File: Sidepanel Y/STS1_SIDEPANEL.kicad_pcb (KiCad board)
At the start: 4 copper layers, 82.8 x 100 mm, 47 parts, among them IC1 TMP112AQDRLRQ1, J1 Conn_01x08, U1 GUVA-C32SM, U11 INA180A4, U12 INA180A4

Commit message: Changed the values of the VCTRL resistors.
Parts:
- R61, R62: value 1M -> 3k
- R71, R72: value 330k -> 1k

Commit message: Updated according to the review from Dhruva.
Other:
- outline, holes or cut-outs redrawn
- board text added: "Y+ v3.0"
- board text removed: "Y+ v2.5"

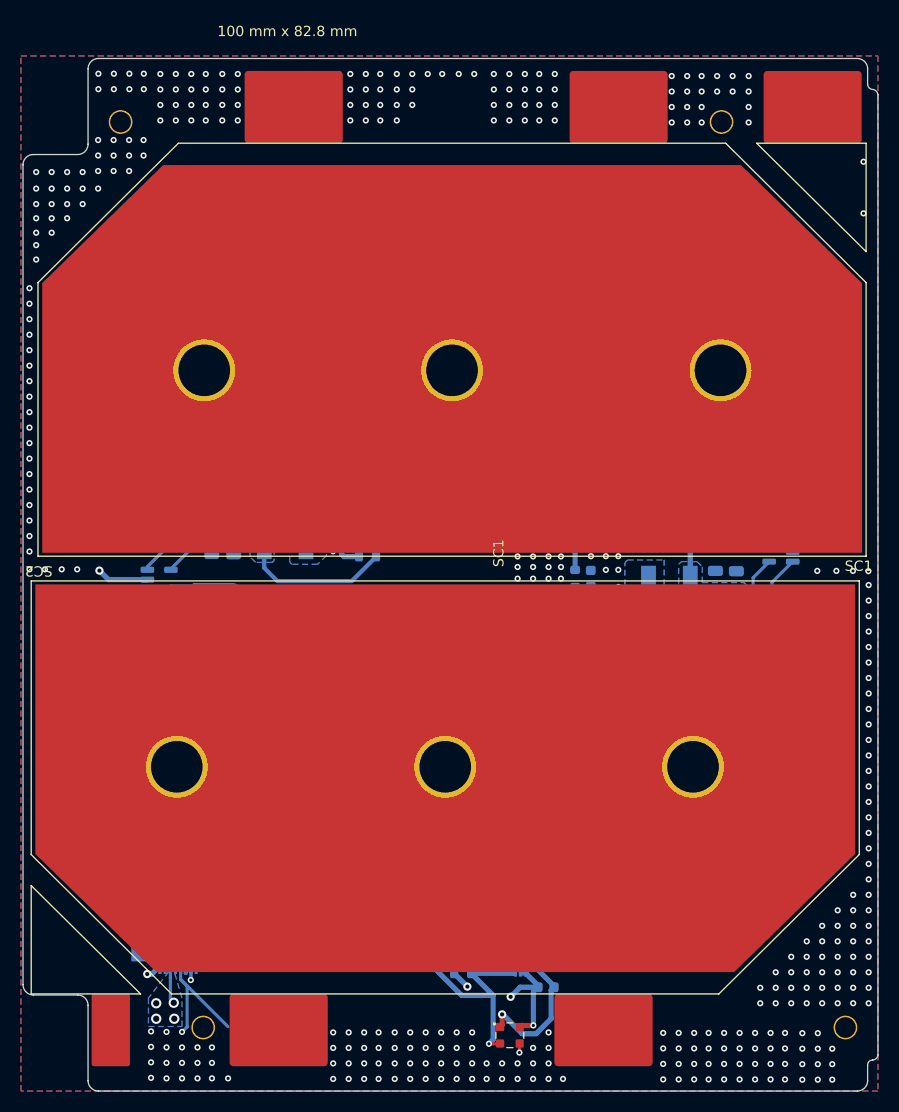
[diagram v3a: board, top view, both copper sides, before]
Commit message: changed all vias from blind to trough and removed the unused pins of the uci connector
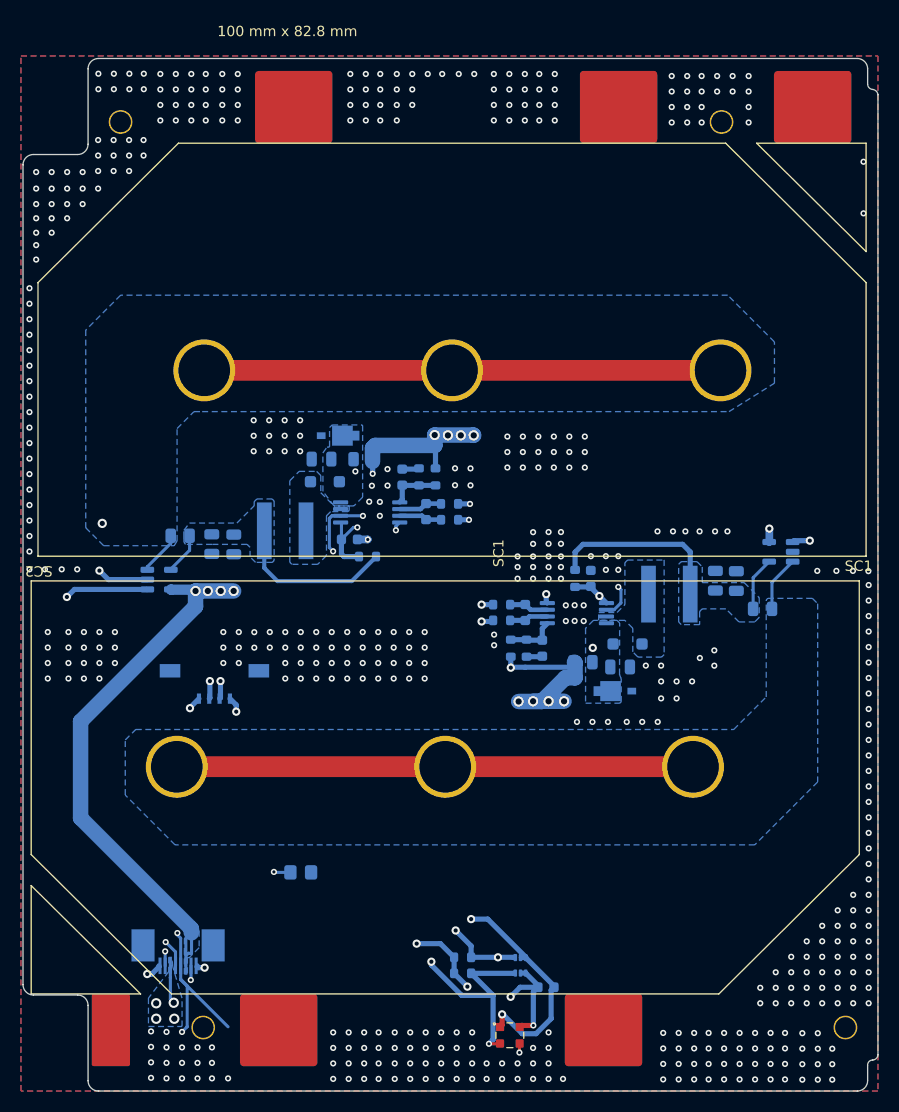
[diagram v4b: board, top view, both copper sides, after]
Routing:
- net /SC2_V+: track 28.3 -> 78.3 mm
- net /SC1_V+: track 66.4 -> 109.0 mm

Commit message: chaned the connectors for the cameras from buttom to top contact
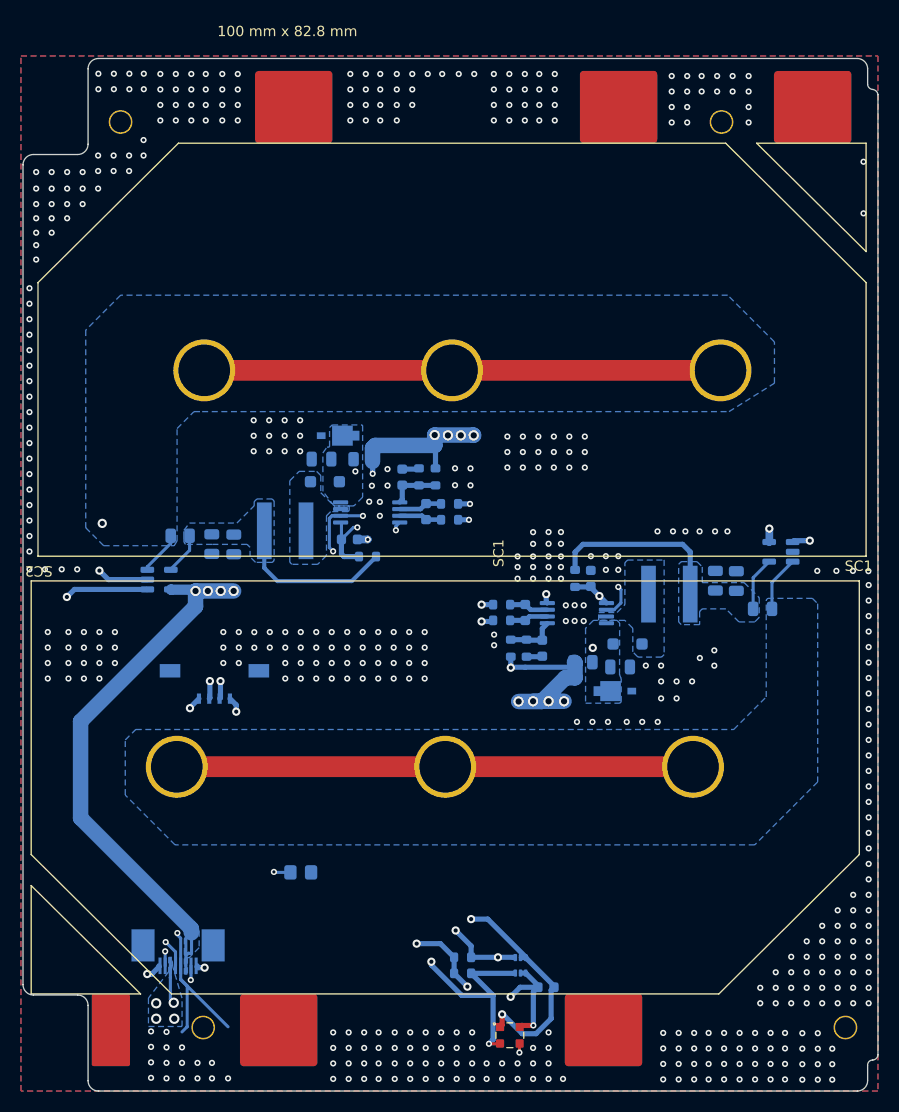
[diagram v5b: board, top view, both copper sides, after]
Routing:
- net GND: vias 505 -> 497
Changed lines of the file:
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@@
-	)
-	(via
-		(at 149.325 45.7)
-		(size 0.6)
-		(drill 0.3)
-		(layers "F.Cu" "B.Cu")
-		(free yes)
-		(net 1)
 	)
 	(via
@@
 	)
 	(via
-		(at 99 133.775)
-		(size 0.6)
-		(drill 0.3)
-		(layers "F.Cu" "B.Cu")
-		(free yes)
-		(net 1)
-	)
-	(via
 		(at 147.925 44.2)
 		(size 0.6)
@@
 	)
 	(via
-		(at 93.875 47.4)
-		(size 0.6)
-		(drill 0.3)
-		(layers "F.Cu" "B.Cu")
-		(free yes)
-		(net 1)
-	)
-	(via
 		(at 152.325 42.7)
 		(size 0.6)
@@
 	)
 	(via
-		(at 149.325 44.2)
-		(size 0.6)
-		(drill 0.3)
-		(layers "F.Cu" "B.Cu")
-		(free yes)
-		(net 1)
-	)
-	(via
 		(at 101.9 138.275)
 		(size 0.6)
@@
 	)
 	(via
-		(at 90.875 47.4)
-		(size 0.6)
-		(drill 0.3)
-		(layers "F.Cu" "B.Cu")
-		(free yes)
-		(net 1)
-	)
-	(via
 		(at 119.5 99.55)
 		(size 0.6)
@@
 	)
 	(via
-		(at 101.9 135.275)
-		(size 0.6)
-		(drill 0.3)
-		(layers "F.Cu" "B.Cu")
-		(free yes)
-		(net 1)
-	)
-	(via
 		(at 145.05 85.3)
 		(size 0.6)
@@
 	)
 	(via
-		(at 100.5 135.275)
-		(size 0.6)
-		(drill 0.3)
-		(layers "F.Cu" "B.Cu")
-		(free yes)
-		(net 1)
-	)
-	(via
 		(at 133.6 42.5)
 		(size 0.6)
@@
 		(size 0.6)
 		(drill 0.3)
-		(layers "F.Cu" "B.Cu")
-		(free yes)
-		(net 1)
-	)
-	(via
-		(at 92.375 47.4)
-		(size 0.6)
-		(drill 0.3)

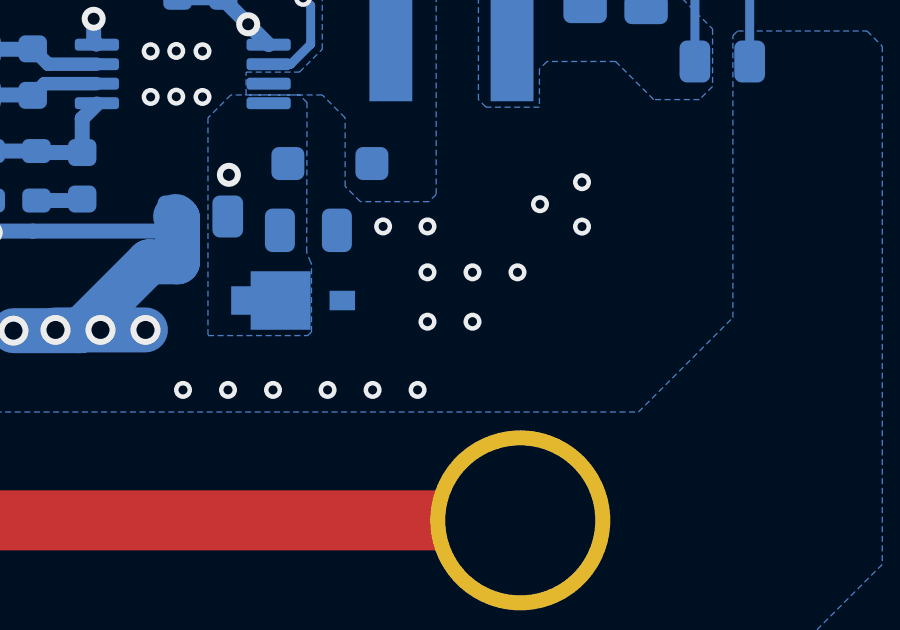
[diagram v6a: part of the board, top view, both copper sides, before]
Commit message: Changed one of the inputs capacitors for all panels with one of 1 uF and lower ESR and moved some traces that were under the inductor.
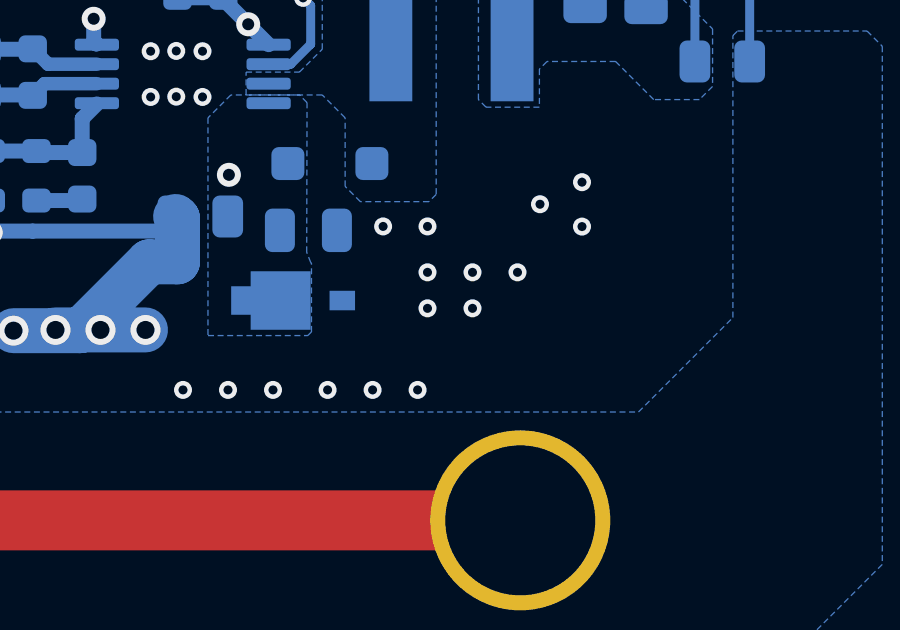
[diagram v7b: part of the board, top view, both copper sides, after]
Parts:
- C61, C62: value 22u -> 1u
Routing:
- net /MPPT1: track 123.3 -> 128.7 mm
- net /SC2_I+: track 96.3 -> 100.7 mm
- net /MPPT2: track 131.0 -> 134.8 mm
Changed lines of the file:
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@@
 			)
 		)
-		(sheetname "Stammblatt")
+		(sheetname "Root")
 		(sheetfile "STS1_SIDEPANEL.kicad_sch")
 		(attr exclude_from_bom)
@@
 		)
 		(property ki_fp_filters "Connector*:*_1x??_*")
-		(sheetname "Stammblatt")
+		(sheetname "Root")
 		(sheetfile "STS1_SIDEPANEL.kicad_sch")
 		(zone_connect 2)
@@
 			)
 		)
-		(sheetname "Stammblatt")
+		(sheetname "Root")
 		(sheetfile "STS1_SIDEPANEL.kicad_sch")
 		(attr smd)
@@
 			)
 		)
-		(property "Value" "22u"
+		(property "Value" "1u"
 			(at 0 -1.68 90)
 			(layer "B.Fab")
@@
 		)
 		(property "Footprint" "Capacitor_SMD:C_0805_2012Metric"
-			(at 0 0 -90)
+			(at 0 0 90)
 			(layer "F.Fab")
 			(hide yes)
@@
 		)
 		(property "Datasheet" ""
-			(at 0 0 -90)
+			(at 0 0 90)
 			(layer "F.Fab")
 			(hide yes)
@@
 			)
 		)
-		(property "Description" ""
-			(at 0 0 -90)
+		(property "Description" "TMK212B7105KGHTR"
+			(at 0 0 90)
 			(layer "F.Fab")
 			(hide yes)
@@
 		)
 		(property ki_fp_filters "*NTC* *Thermistor* PIN?ARRAY* bornier* *Terminal?Block* R_*")
-		(sheetname "Stammblatt")
+		(sheetname "Root")
 		(sheetfile "STS1_SIDEPANEL.kicad_sch")
 		(attr smd)
@@
 			)
 		)
-		(property "Value" "22u"
+		(property "Value" "1u"
 			(at 0 -1.68 90)
 			(layer "B.Fab")
@@
 			)
 		)
-		(property "Description" ""
+		(property "Description" "TMK212B7105KGHTR"
 			(at 0 0 90)
 			(layer "F.Fab")
@@
 	)
 	(via
-		(at 146.9 101.475)
+		(at 146.9 101.03)
 		(size 0.6)
 		(drill 0.3)
@@
 	)
 	(via
-		(at 145.4 101.475)
+		(at 145.4 101.03)
 		(size 0.6)
 		(drill 0.3)
@@
 	)
 	(segment
-		(start 114.54 78.087944)
-		(end 114.54 80.96)
-		(width 1.5)
-		(layer "In2.Cu")
-		(net 7)
-	)
-	(segment
-		(start 127.22 75.97)
-		(end 116.657944 75.97)
+		(start 113.3 91.07)
+		(end 104 91.07)
 		(width 1.5)
 		(layer "In2.Cu")
@@
 	)
 	(segment
+		(start 127.22 75.97)
+		(end 116.657944 75.97)
+		(width 1.5)
+		(layer "In2.Cu")
+		(net 7)
+	)
+	(segment
+		(start 114.884 86.713233)
+		(end 114.884 89.486)
+		(width 1.5)
+		(layer "In2.Cu")
+		(net 7)
+	)
+	(segment
+		(start 116.657944 75.97)
+		(end 114.54 78.087944)
+		(width 1.5)
+		(layer "In2.Cu")
+		(net 7)
+	)
+	(segment
 		(start 118.01 78.07)
 		(end 117.44 78.64)
@@
 	)
 	(segment
-		(start 127.25 76)
-		(end 127.22 75.97)
+		(start 114.54 86.369233)
+		(end 114.884 86.713233)
 		(width 1.5)
 		(layer "In2.Cu")
@@
 	)
 	(segment
-		(start 116.657944 75.97)
-		(end 114.54 78.087944)
-		(width 1.5)
-		(layer "In2.Cu")
-		(net 7)
-	)
-	(segment
 		(start 126.89 82.64)
 		(end 128.04 82.64)
@@
 	)
 	(segment
-		(start 114.54 80.96)
-		(end 104.43 91.07)
+		(start 127.25 76)
+		(end 127.22 75.97)
 		(width 1.5)
 		(layer "In2.Cu")
@@
 	)
 	(segment
-		(start 104.43 91.07)
-		(end 104 91.07)
+		(start 114.54 78.087944)
+		(end 114.54 86.369233)
+		(width 1.5)
+		(layer "In2.Cu")
+		(net 7)
+	)
+	(segment
+		(start 114.884 89.486)
+		(end 113.3 91.07)
 		(width 1.5)
 		(layer "In2.Cu")
@@
 	)
 	(segment
+		(start 158.47 94.12)
+		(end 149.82 102.77)
+		(width 0.75)
+		(layer "In2.Cu")
+		(net 8)
+	)
+	(segment
 		(start 128.8 98.5)
 		(end 127.8605 97.5605)
@@
 	)
 	(segment
-		(start 160.773 85.794141)
-		(end 160.773 86.834887)
+		(start 160.773 86.834887)
+		(end 158.47 89.137887)
 		(width 0.75)
 		(layer "In2.Cu")
@@
 	)
 	(segment
-		(start 147.686726 90.93)
-		(end 136.866726 101.75)
+		(start 149.82 102.77)
+		(end 137.02 102.77)
 		(width 0.75)
 		(layer "In2.Cu")
@@
 	)
 	(segment
-		(start 160.008859 85.03)
-		(end 160.773 85.794141)
+		(start 160.773 85.794141)
+		(end 160.773 86.834887)
 		(width 0.75)
 		(layer "In2.Cu")
@@
 	)
 	(segment
+		(start 155.88 85.03)
+		(end 160.008859 85.03)
+		(width 0.75)
+		(layer "In2.Cu")
+		(net 8)
+	)
+	(segment
 		(start 123.3 130)
 		(end 131.525 121.775)
@@
 	)
 	(segment
-		(start 136.866726 101.75)
-		(end 136 101.75)
+		(start 158.47 89.137887)
+		(end 158.47 94.12)
 		(width 0.75)
 		(layer "In2.Cu")
@@
 	)
 	(segment
-		(start 160.773 86.834887)
-		(end 156.677887 90.93)
-		(width 0.75)
+		(start 135.975 101.775)
+		(end 136 101.75)
+		(width 1.5)
 		(layer "In2.Cu")
 		(net 8)
 	)
 	(segment
-		(start 135.975 101.775)
+		(start 137.02 102.77)
 		(end 136 101.75)
-		(width 1.5)
+		(width 0.75)
 		(layer "In2.Cu")
 		(net 8)
@@
 	)
 	(segment
-		(start 155.88 85.03)
-		(end 160.008859 85.03)
+		(start 160.008859 85.03)
+		(end 160.773 85.794141)
 		(width 0.75)
 		(layer "In2.Cu")
@@
 	)
 	(segment
-		(start 156.677887 90.93)
-		(end 147.686726 90.93)
-		(width 0.75)
-		(layer "In2.Cu")
-		(net 8)
-	)
-	(segment
 		(start 130.842 98.5)
 		(end 130.8865 98.4555)
@@
 	)
 	(segment
-		(start 159.798 86.198)
-		(end 159.798 86.643161)
+		(start 159.798 86.643161)
+		(end 157.645 88.796161)
 		(width 0.5)
 		(layer "In2.Cu")
@@
 	)
 	(segment
-		(start 156.416161 90.025)
-		(end 147.425 90.025)
+		(start 104.05 128.8)
+		(end 101.222998 125.972998)
 		(width 0.5)
 		(layer "In2.Cu")
@@
 	)
 	(segment
-		(start 104.05 128.8)
-		(end 101.222998 125.972998)
+		(start 137.2 101.252944)
+		(end 136.497056 100.55)
 		(width 0.5)
 		(layer "In2.Cu")
@@
 	)
 	(segment
-		(start 131.602944 100.075)
-		(end 130.325 101.352944)
+		(start 135.502944 100.55)
+		(end 135.477944 100.575)
 		(width 0.5)
 		(layer "In2.Cu")
@@
 	)
 	(segment
-		(start 159.798 86.643161)
-		(end 156.416161 90.025)
+		(start 157.645 93.778274)
+		(end 149.478274 101.945)
 		(width 0.5)
 		(layer "In2.Cu")
@@
 	)
 	(segment
-		(start 122.802944 128.8)
-		(end 104.05 128.8)
+		(start 136.497056 100.55)
+		(end 135.502944 100.55)
+		(width 0.5)
+		(layer "In2.Cu")
+		(net 9)
+	)
+	(segment
+		(start 137.361726 101.945)
+		(end 137.2 101.783274)
 		(width 0.5)
 		(layer "In2.Cu")
@@
 	)
 	(segment
+		(start 131.102944 100.575)
+		(end 130.325 101.352944)
+		(width 0.5)
+		(layer "In2.Cu")
+		(net 9)
+	)
+	(segment
+		(start 122.802944 128.8)
+		(end 104.05 128.8)
+		(width 0.5)
+		(layer "In2.Cu")
+		(net 9)
+	)
+	(segment
+		(start 135.477944 100.575)
+		(end 131.102944 100.575)
+		(width 0.5)
+		(layer "In2.Cu")
+		(net 9)
+	)
+	(segment
+		(start 159.798 86.198)
+		(end 159.798 86.643161)
+		(width 0.5)
+		(layer "In2.Cu")
+		(net 9)
+	)
+	(segment
+		(start 137.2 101.783274)
+		(end 137.2 101.252944)
+		(width 0.5)
+		(layer "In2.Cu")
+		(net 9)
+	)
+	(segment
 		(start 101.222998 125.972998)
 		(end 97.37 125.972998)
@@
 	)
 	(segment
-		(start 147.425 90.025)
-		(end 137.375 100.075)
+		(start 157.645 88.796161)
+		(end 157.645 93.778274)
 		(width 0.5)
 		(layer "In2.Cu")
@@
 	)
 	(segment
-		(start 137.375 100.075)
-		(end 131.602944 100.075)
+		(start 149.478274 101.945)
+		(end 137.361726 101.945)
 		(width 0.5)
 		(layer "In2.Cu")
